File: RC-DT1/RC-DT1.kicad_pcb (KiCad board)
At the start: 2 copper layers, 100 x 100 mm, 13 parts

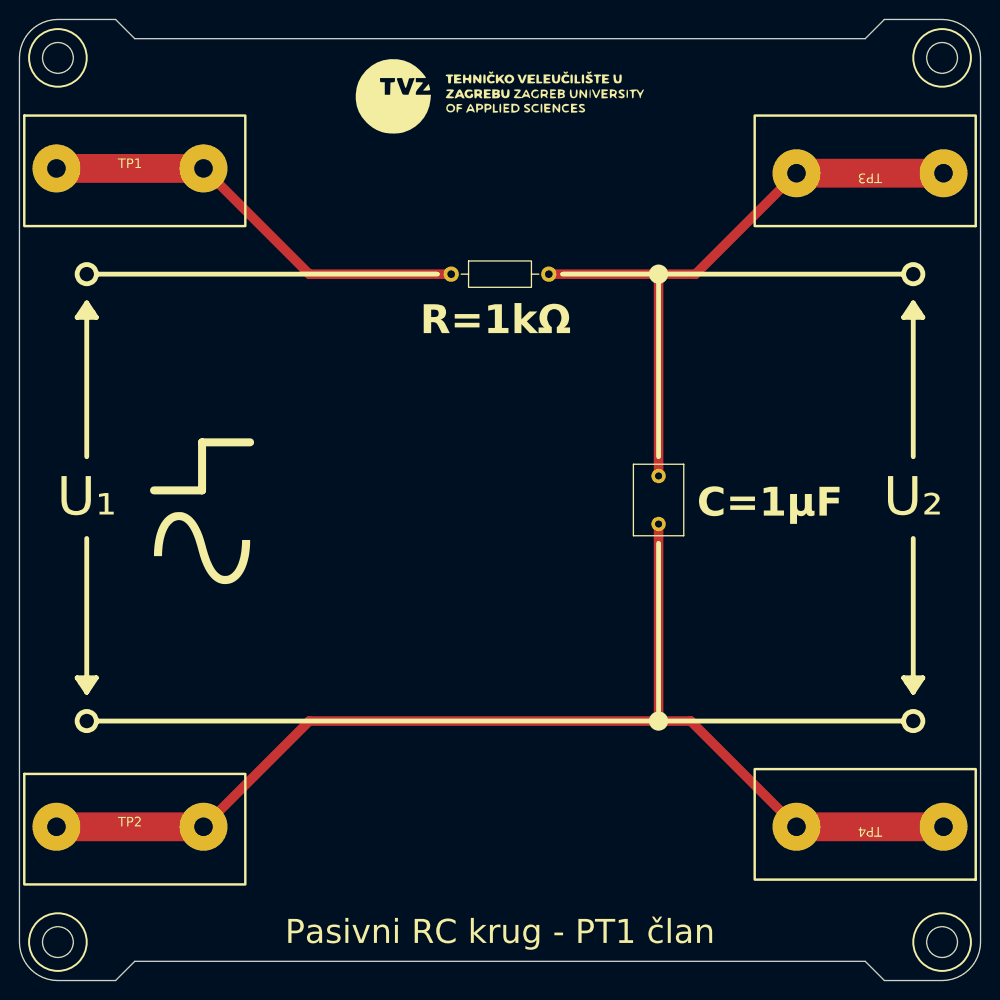
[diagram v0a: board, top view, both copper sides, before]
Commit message: DT1 added
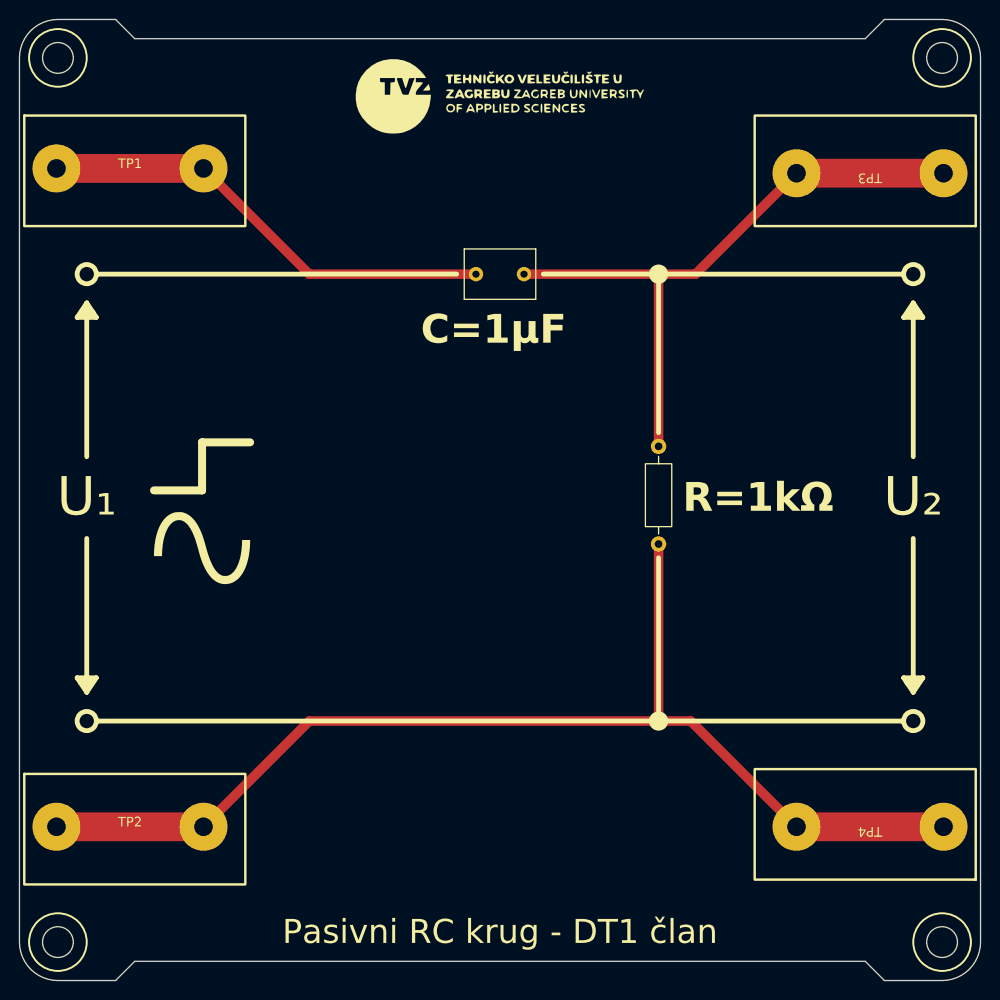
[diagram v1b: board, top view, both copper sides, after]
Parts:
- moved R1 35.4 mm to (162.5, 110.6), turned to 90 degrees
- moved C1 28.3 mm to (143.5, 82.5), turned to 0 degrees
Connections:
- R1 pad 2: Net-(C1-Pad1) -> Net-(C1-Pad2)
- TP1 pad 1: Net-(R1-Pad1) -> Net-(C1-Pad1)
- TP2 pad 1: Net-(C1-Pad2) -> Net-(R1-Pad1)
- TP3 pad 1: Net-(C1-Pad1) -> Net-(C1-Pad2)
- TP4 pad 1: Net-(C1-Pad2) -> Net-(R1-Pad1)
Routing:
- net Net-(R1-Pad1): track 45.7 -> 119.8 mm
- net Net-(C1-Pad2): track 121.9 -> 65.9 mm
- net Net-(C1-Pad1): track 66.4 -> 48.2 mm
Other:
- board text added: "Pasivni RC krug - DT1 član"
- board text removed: "Pasivni RC krug - PT1 član"
